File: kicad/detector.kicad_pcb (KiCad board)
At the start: 4 copper layers, 38.5 x 35.8 mm, 46 parts, among them J1 Conn_01x05_Male, J2 Conn_01x05_Male, M2.5 MountingHole_2.7mm_M2.5_ISO73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, U1 LT1761-5, U2 LT1964-5, U3 REF5010ID, U4 OPA2197xD, U5 OPA2197xD

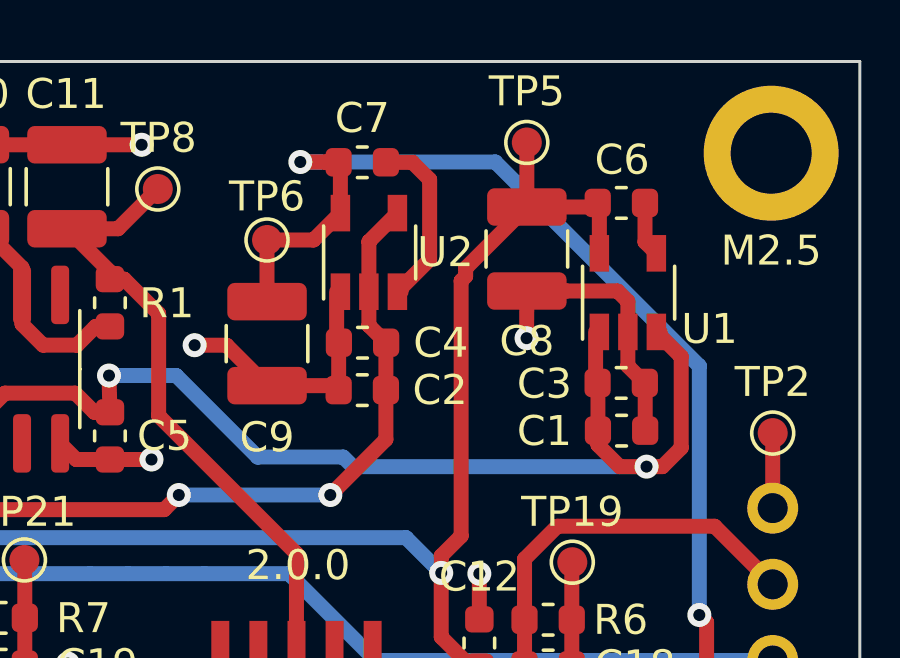
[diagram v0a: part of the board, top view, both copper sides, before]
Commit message: added fill zones around voltage regulators
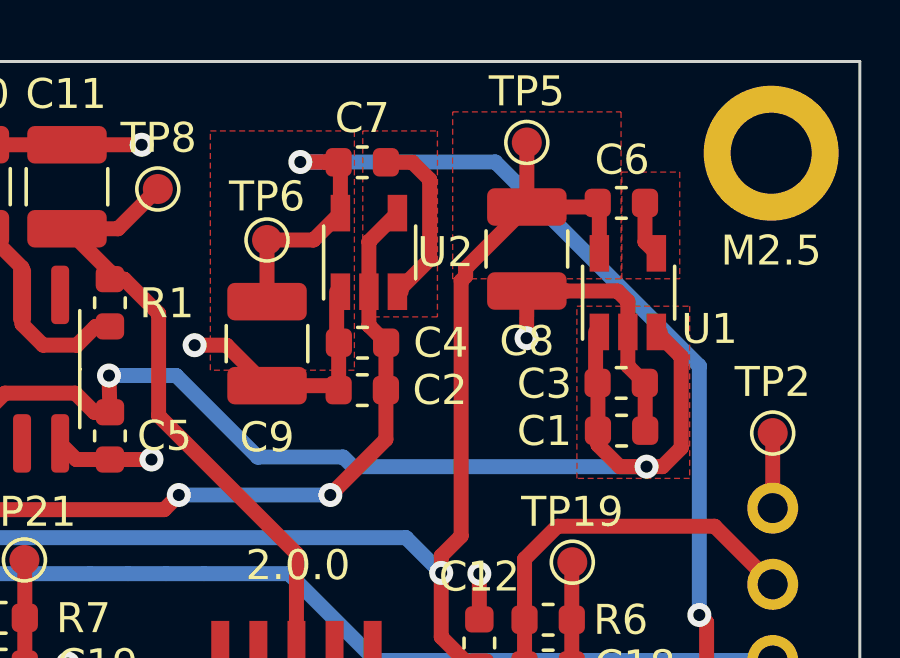
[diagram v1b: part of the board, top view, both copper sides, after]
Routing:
- added copper zone on F.Cu, net +12V
- added copper zone on F.Cu, net +5V
- added copper zone on F.Cu, net -5V
- added copper zone on F.Cu, net Net-(C6-Pad1)
- added copper zone on F.Cu, net Net-(C7-Pad2)

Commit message: move detector power supplies around (wip)
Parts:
- moved C2 15.7 mm to (154.1, 116.6), turned to 180 degrees
- moved TP7 15.3 mm to (166.3, 122.0), turned to 180 degrees
- moved C10 15.0 mm to (167.6, 124.8), turned to 0 degrees
- moved C7 14.4 mm to (154.1, 124.2), turned to 180 degrees
- moved C4 14.2 mm to (154.1, 118.1), turned to 180 degrees
- moved C11 14.0 mm to (167.6, 128.0), turned to 0 degrees
- moved U2 13.4 mm to (153.9, 121.1), turned to 270 degrees
- moved TP8 13.3 mm to (164.9, 131.2), turned to 270 degrees
- moved TP5 10.6 mm to (176.8, 126.9), turned to 270 degrees
- moved C1 9.75 mm to (173.6, 117.3), turned to 180 degrees
- moved C9 8.80 mm to (157.3, 118.1), turned to 270 degrees
- moved R1 8.59 mm to (163.8, 129.4), turned to 180 degrees
- moved TP6 6.72 mm to (157.3, 121.6), turned to 180 degrees
- moved C3 6.67 mm to (173.6, 118.9), turned to 180 degrees
- moved U3 6.56 mm to (161.6, 125.9), turned to 0 degrees
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- renumbered TP2 to GND
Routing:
- net +5V: track 53.1 -> 26.2 mm, vias 2 -> 0
- net +12V: track 58.3 -> 33.8 mm, vias 2 -> 0
- net Net-(C11-Pad1): track 21.3 -> 7.36 mm
- net -5V: track 72.6 -> 84.6 mm
- net -12V: track 28.7 -> 20.1 mm, vias 2 -> 0
- net /-Y1: track 36.8 -> 42.9 mm
- net /-X2: track 32.9 -> 38.1 mm, vias 1 -> 2
- net Net-(C10-Pad1): track 13.7 -> 8.51 mm
- net GND: track 50.2 -> 46.1 mm, vias 11 -> 9
- net /-X1: track 21.1 -> 17.4 mm
- net Net-(C19-Pad2): track 16.8 -> 14.8 mm
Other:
- board text added: "2.0"

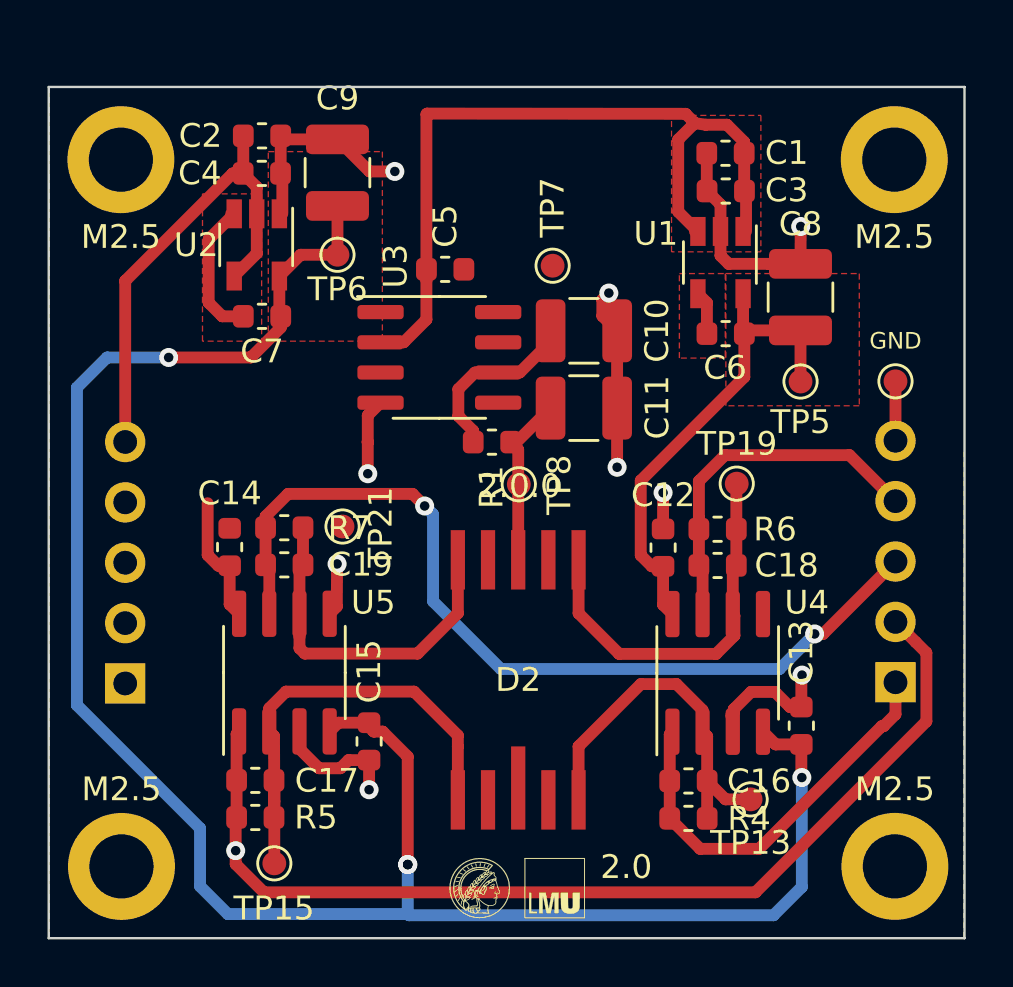
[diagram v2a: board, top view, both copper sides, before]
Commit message: added mounting holes to eeschema, replaced mounting holes with pad
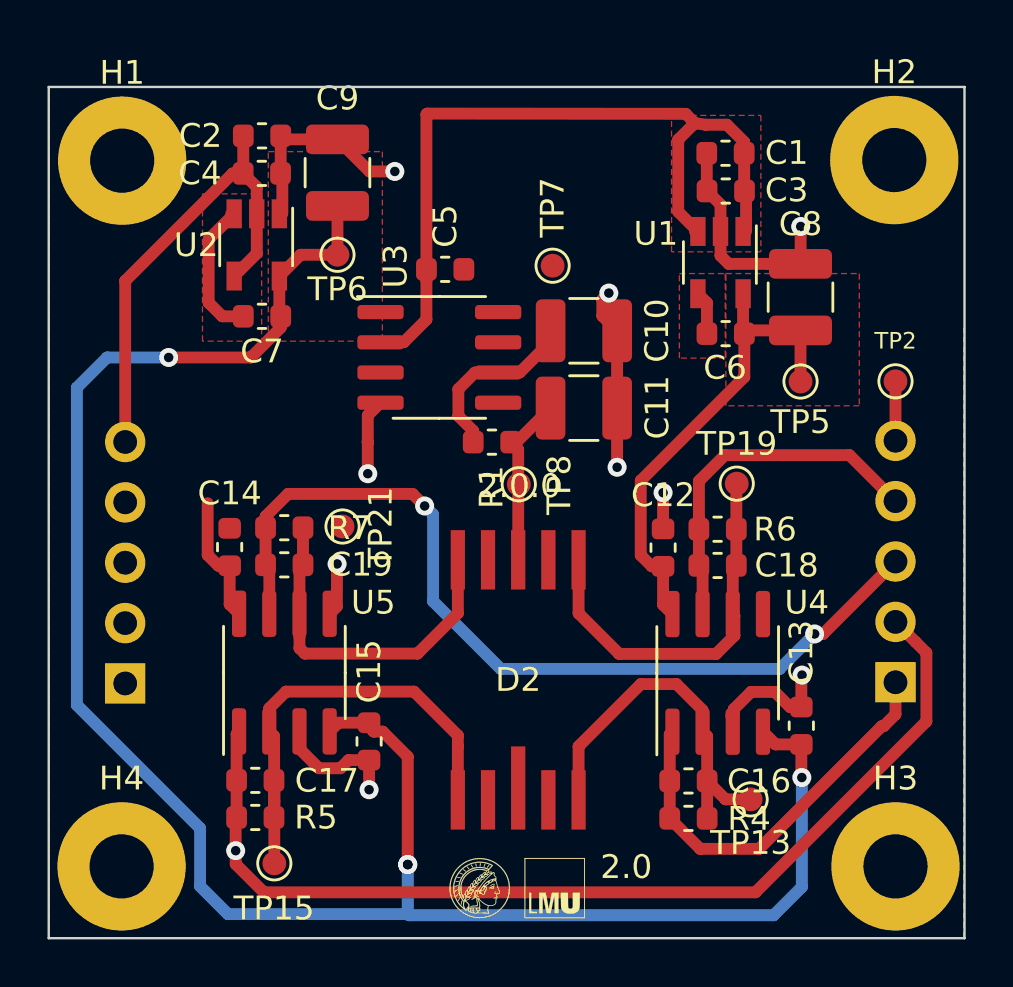
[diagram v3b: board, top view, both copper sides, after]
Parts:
- removed M2.5 (x4): MountingHole_2.7mm_M2.5_ISO7380_Pad, MountingHole:MountingHole_2.7mm_M2.5_ISO7380_Pad
- added H1: MountingHole_Pad, MountingHole:MountingHole_2.7mm_M2.5_Pad, F.Cu at (148.2, 117.6)
- added H2: MountingHole_Pad, MountingHole:MountingHole_2.7mm_M2.5_Pad, F.Cu at (180.7, 117.6)
- added H3: MountingHole_Pad, MountingHole:MountingHole_2.7mm_M2.5_Pad, F.Cu at (180.7, 147.3)
- added H4: MountingHole_Pad, MountingHole:MountingHole_2.7mm_M2.5_Pad, F.Cu at (148.2, 147.3)
- R4, R5, R6, R7: value 6k -> 6.04k
- renumbered GND to TP2
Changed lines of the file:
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@@
-(kicad_pcb (version 20171130) (host pcbnew 5.1.5)
+(kicad_pcb (version 20171130) (host pcbnew "(5.1.5-0-10_14)")
   (general
     (thickness 1.6)
@@
     (add_net "Net-(U3-Pad7)")
     (add_net "Net-(U3-Pad8)")
+  )
+  (module MountingHole:MountingHole_2.7mm_M2.5_Pad (layer F.Cu)
+    (at 148.1836 147.2946)
+    (descr "Mounting Hole 2.7mm, M2.5")
+    (tags "mounting hole 2.7mm m2.5")
+    (attr virtual)
+    (fp_text reference H4 (at 0 -3.7) (layer F.SilkS)
+      (effects (font (size 1 1) (thickness 0.15)))
+    )
+    (fp_text value MountingHole_Pad (at 0 3.7) (layer F.Fab)
+      (effects (font (size 1 1) (thickness 0.15)))
+    )
+    (fp_circle (center 0 0) (end 2.95 0) (layer F.CrtYd) (width 0.05))
+    (fp_circle (center 0 0) (end 2.7 0) (layer Cmts.User) (width 0.15))
+    (fp_text user %R (at 0.3 0) (layer F.Fab)
+      (effects (font (size 1 1) (thickness 0.15)))
+    )
+    (pad 1 thru_hole circle (at 0 0) (size 5.4 5.4) (drill 2.7) (layers *.Cu *.Mask)
+      (net 1 GND))
+  )
+  (module MountingHole:MountingHole_2.7mm_M2.5_Pad (layer F.Cu)
+    (at 180.7464 147.2946)
+    (descr "Mounting Hole 2.7mm, M2.5")
+    (tags "mounting hole 2.7mm m2.5")
+    (attr virtual)
+    (fp_text reference H3 (at 0 -3.7) (layer F.SilkS)
+      (effects (font (size 1 1) (thickness 0.15)))
+    )
+    (fp_text value MountingHole_Pad (at 0 3.7) (layer F.Fab)
+      (effects (font (size 1 1) (thickness 0.15)))
+    )
+    (fp_circle (center 0 0) (end 2.95 0) (layer F.CrtYd) (width 0.05))
+    (fp_circle (center 0 0) (end 2.7 0) (layer Cmts.User) (width 0.15))
+    (fp_text user %R (at 0.3 0) (layer F.Fab)
+      (effects (font (size 1 1) (thickness 0.15)))
+    )
+    (pad 1 thru_hole circle (at 0 0) (size 5.4 5.4) (drill 2.7) (layers *.Cu *.Mask)
+      (net 1 GND))
+  )
+  (module MountingHole:MountingHole_2.7mm_M2.5_Pad (layer F.Cu)
+    (at 180.6956 117.5766)
+    (descr "Mounting Hole 2.7mm, M2.5")
+    (tags "mounting hole 2.7mm m2.5")
+    (attr virtual)
+    (fp_text reference H2 (at 0 -3.7) (layer F.SilkS)
+      (effects (font (size 1 1) (thickness 0.15)))
+    )
+    (fp_text value MountingHole_Pad (at 0 3.7) (layer F.Fab)
+      (effects (font (size 1 1) (thickness 0.15)))
+    )
+    (fp_circle (center 0 0) (end 2.95 0) (layer F.CrtYd) (width 0.05))
+    (fp_circle (center 0 0) (end 2.7 0) (layer Cmts.User) (width 0.15))
+    (fp_text user %R (at 0.3 0) (layer F.Fab)
+      (effects (font (size 1 1) (thickness 0.15)))
+    )
+    (pad 1 thru_hole circle (at 0 0) (size 5.4 5.4) (drill 2.7) (layers *.Cu *.Mask)
+      (net 1 GND))
+  )
+  (module MountingHole:MountingHole_2.7mm_M2.5_Pad (layer F.Cu)
+    (at 148.209 117.602)
+    (descr "Mounting Hole 2.7mm, M2.5")
+    (tags "mounting hole 2.7mm m2.5")
+    (attr virtual)
+    (fp_text reference H1 (at 0 -3.7) (layer F.SilkS)
+      (effects (font (size 1 1) (thickness 0.15)))
+    )
+    (fp_text value MountingHole_Pad (at 0 3.7) (layer F.Fab)
+      (effects (font (size 1 1) (thickness 0.15)))
+    )
+    (fp_circle (center 0 0) (end 2.95 0) (layer F.CrtYd) (width 0.05))
+    (fp_circle (center 0 0) (end 2.7 0) (layer Cmts.User) (width 0.15))
+    (fp_text user %R (at 0.3 0) (layer F.Fab)
+      (effects (font (size 1 1) (thickness 0.15)))
+    )
+    (pad 1 thru_hole circle (at 0 0) (size 5.4 5.4) (drill 2.7) (layers *.Cu *.Mask)
+      (net 1 GND))
   )
   (module Package_SO:SOIC-8_3.9x4.9mm_P1.27mm (layer F.Cu)
@@
     (tags "test point SMD pad")
     (attr virtual)
-    (fp_text reference GND (at -1.7 0 180) (layer F.SilkS)
+    (fp_text reference TP2 (at -1.7 0 180) (layer F.SilkS)
       (effects (font (size 0.7 0.7) (thickness 0.1)))
     )
@@
     (pad 1 smd circle (at 0 0 270) (size 1 1) (layers F.Cu F.Mask)
       (net 1 GND))
-  )
-  (module MountingHole:MountingHole_2.7mm_M2.5_ISO7380_Pad (layer F.Cu)
-    (at 180.6956 117.5574 180)
-    (descr "Mounting Hole 2.7mm, M2.5, ISO7380")
-    (tags "mounting hole 2.7mm m2.5 iso7380")
-    (attr virtual)
-    (fp_text reference M2.5 (at 0 -3.25) (layer F.SilkS)
-      (effects (font (size 1 1) (thickness 0.15)))
-    )
-    (fp_text value MountingHole_2.7mm_M2.5_ISO7380_Pad (at 0 3.25) (layer F.Fab)
-      (effects (font (size 1 1) (thickness 0.15)))
-    )
-    (fp_text user %R (at 0.3 0) (layer F.Fab)
-      (effects (font (size 1 1) (thickness 0.15)))
-    )
-    (fp_circle (center 0 0) (end 2.25 0) (layer Cmts.User) (width 0.15))
-    (fp_circle (center 0 0) (end 2.5 0) (layer F.CrtYd) (width 0.05))
-    (pad 1 thru_hole circle (at 0 0 180) (size 4.5 4.5) (drill 2.7) (layers *.Cu *.Mask))
-  )
-  (module MountingHole:MountingHole_2.7mm_M2.5_ISO7380_Pad (layer F.Cu)
-    (at 148.1542 117.5596 180)
-    (descr "Mounting Hole 2.7mm, M2.5, ISO7380")
-    (tags "mounting hole 2.7mm m2.5 iso7380")
-    (attr virtual)
-    (fp_text reference M2.5 (at 0 -3.25) (layer F.SilkS)
-      (effects (font (size 1 1) (thickness 0.15)))
-    )
-    (fp_text value MountingHole_2.7mm_M2.5_ISO7380_Pad (at 0 3.25) (layer F.Fab)
-      (effects (font (size 1 1) (thickness 0.15)))
-    )
-    (fp_text user %R (at 0.3 0) (layer F.Fab)
-      (effects (font (size 1 1) (thickness 0.15)))
-    )
-    (fp_circle (center 0 0) (end 2.25 0) (layer Cmts.User) (width 0.15))
-    (fp_circle (center 0 0) (end 2.5 0) (layer F.CrtYd) (width 0.05))
-    (pad 1 thru_hole circle (at 0 0 180) (size 4.5 4.5) (drill 2.7) (layers *.Cu *.Mask))
-  )
-  (module MountingHole:MountingHole_2.7mm_M2.5_ISO7380_Pad (layer F.Cu)
-    (at 148.1796 147.2968)
-    (descr "Mounting Hole 2.7mm, M2.5, ISO7380")
-    (tags "mounting hole 2.7mm m2.5 iso7380")
-    (attr virtual)
-    (fp_text reference M2.5 (at 0 -3.25) (layer F.SilkS)
-      (effects (font (size 1 1) (thickness 0.15)))
-    )
-    (fp_text value MountingHole_2.7mm_M2.5_ISO7380_Pad (at 0 3.25) (layer F.Fab)
-      (effects (font (size 1 1) (thickness 0.15)))
-    )
-    (fp_circle (center 0 0) (end 2.5 0) (layer F.CrtYd) (width 0.05))
-    (fp_circle (center 0 0) (end 2.25 0) (layer Cmts.User) (width 0.15))
-    (fp_text user %R (at 0.3 0) (layer F.Fab)
-      (effects (font (size 1 1) (thickness 0.15)))
-    )
-    (pad 1 thru_hole circle (at 0 0) (size 4.5 4.5) (drill 2.7) (layers *.Cu *.Mask))
-  )
-  (module MountingHole:MountingHole_2.7mm_M2.5_ISO7380_Pad (layer F.Cu)
-    (at 180.721 147.2946)
-    (descr "Mounting Hole 2.7mm, M2.5, ISO7380")
-    (tags "mounting hole 2.7mm m2.5 iso7380")
-    (attr virtual)
-    (fp_text reference M2.5 (at 0 -3.25) (layer F.SilkS)
-      (effects (font (size 1 1) (thickness 0.15)))
-    )
-    (fp_text value MountingHole_2.7mm_M2.5_ISO7380_Pad (at 0 3.25) (layer F.Fab)
-      (effects (font (size 1 1) (thickness 0.15)))
-    )
-    (fp_circle (center 0 0) (end 2.5 0) (layer F.CrtYd) (width 0.05))
-    (fp_circle (center 0 0) (end 2.25 0) (layer Cmts.User) (width 0.15))
-    (fp_text user %R (at 0.3 0) (layer F.Fab)
-      (effects (font (size 1 1) (thickness 0.15)))
-    )
-    (pad 1 thru_hole circle (at 0 0) (size 4.5 4.5) (drill 2.7) (layers *.Cu *.Mask))
   )
   (module Capacitor_SMD:C_1210_3225Metric (layer F.Cu)
@@
       (effects (font (size 1 1) (thickness 0.15)))
     )
-    (fp_text value 6k (at 0 1.43) (layer F.Fab)
+    (fp_text value 6.04k (at 0 1.43) (layer F.Fab)
       (effects (font (size 1 1) (thickness 0.15)))
     )
@@
       (effects (font (size 1 1) (thickness 0.15)))
     )
-    (fp_text value 6k (at 0 1.43) (layer F.Fab)
+    (fp_text value 6.04k (at 0 1.43) (layer F.Fab)
       (effects (font (size 1 1) (thickness 0.15)))
     )
@@
       (effects (font (size 1 1) (thickness 0.15)))
     )
-    (fp_text value 6k (at 0 1.43) (layer F.Fab)
+    (fp_text value 6.04k (at 0 1.43) (layer F.Fab)
       (effects (font (size 1 1) (thickness 0.15)))
     )
@@
       (effects (font (size 1 1) (thickness 0.15)))
     )
-    (fp_text value 6k (at 0 1.43) (layer F.Fab)
-      (effects (font (size 1 1) (thickness 0.15)))
-    )
+    (fp_text value 6.04k (at 0 1.43) (layer F.Fab)
+      (effects (font (size 1 1) (thickness 0.15)))
+    )

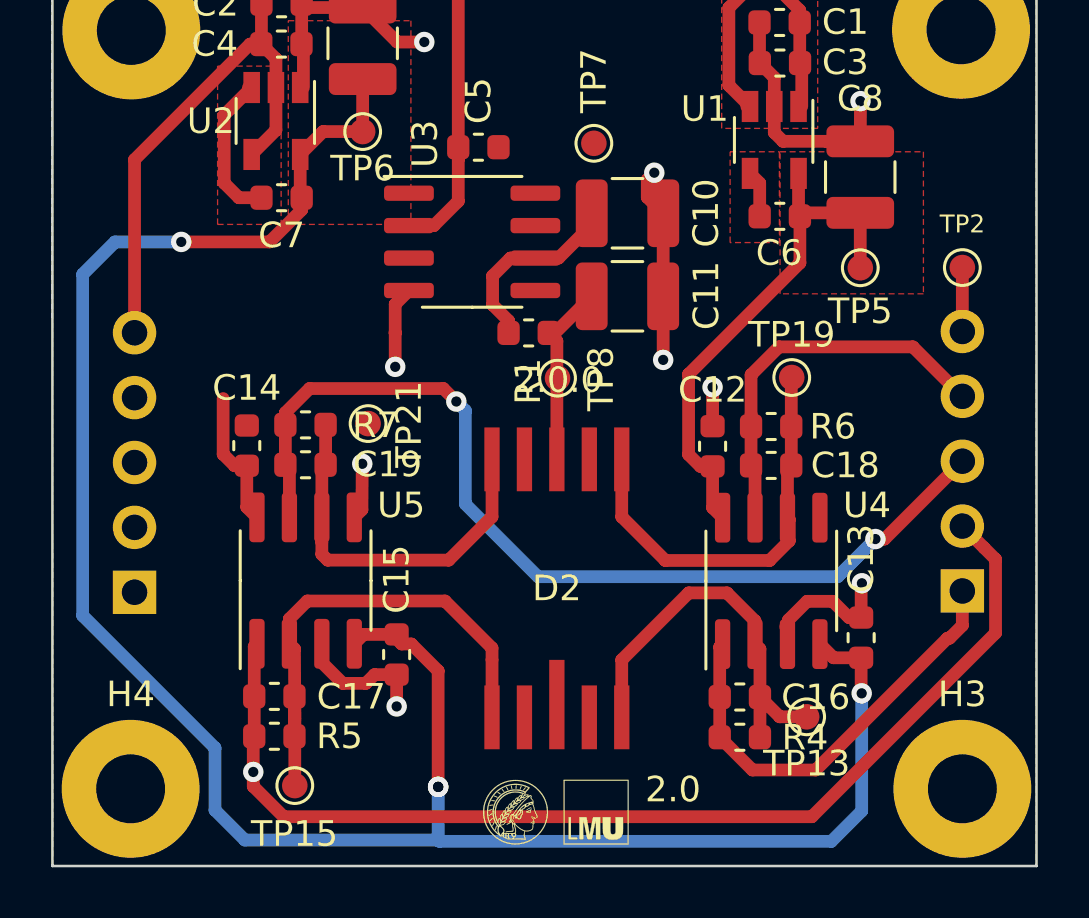
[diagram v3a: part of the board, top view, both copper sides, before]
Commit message: changed header shield pins for improved detector routing
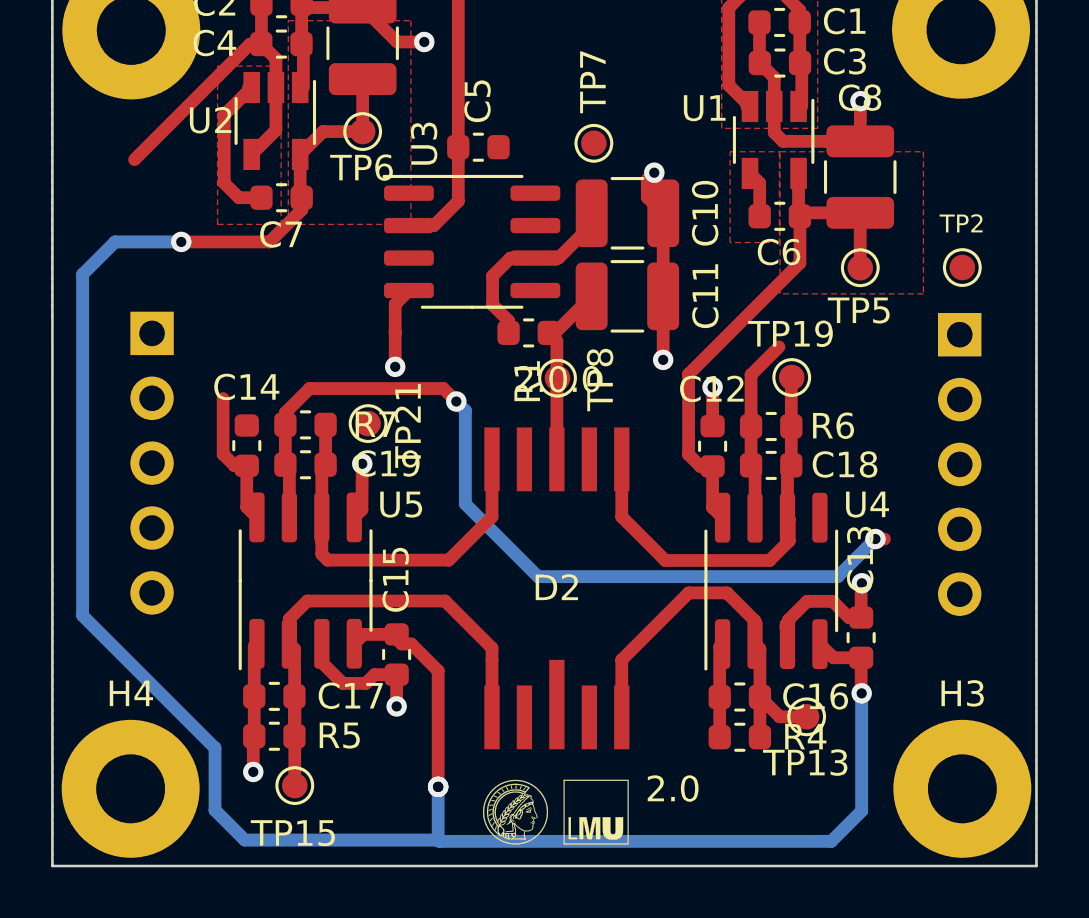
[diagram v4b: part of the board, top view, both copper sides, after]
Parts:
- moved J1 10.2 mm to (149.0, 129.5), turned to 180 degrees
- moved J2 10.0 mm to (180.6, 129.5), turned to 180 degrees
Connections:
- J1 pad 1: +12V -> -12V
- J1 pad 4: GND -> /-X2
- J1 pad 5: -12V -> /-Y1
- J2 pad 1: /-X1 -> +12V
- J2 pad 2: /-Y1 -> GND
- J2 pad 3: /-X2 -> GND
- J2 pad 5: GND -> /-X1
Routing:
- net /-Y1: track 42.9 -> 5.08 mm
- net /-X1: track 17.4 -> 3.69 mm
- net /-Y2: track 15.2 -> 7.21 mm
- net -12V: track 20.1 -> 13.4 mm
- net /-X2: track 38.1 -> 33.8 mm
- net GND: track 46.1 -> 43.6 mm
